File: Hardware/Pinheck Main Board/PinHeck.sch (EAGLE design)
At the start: 521 parts, among them IC2 PIC32MX795F512L-80I/PT, IC3 CD74HCT244E, IC4 CD74HCT244E, IC5 ULN2803A, J1 N/A, U1 P8X32A-Q44, U10 74HCT2G04GV,125, U11 74HC165D-Q100,118, U12 74HC165D-Q100,118, U13 CAT24M01LI-G, U14 MC74HC08ADR2G, U15 MC74HC08ADR2G, U16 MC74HC08ADR2G, U17 MC74HC08ADR2G, U18 MC74HC08ADR2G, U19 MC74HC08ADR2G, U2 DS1340Z-33+, U20 TIP107, U21 TIP107, U22 TIP107, U23 TIP107, U24 TIP107, U25 TIP107, U26 TIP107, U27 TIP107, U28 TIP102, U29 TIP102, U3 CD74HC595M96, U30 TIP102, U31 TIP102, U32 TIP102, U33 TIP102, U34 TIP102, U35 TIP102, U36 WS2801, U38 WS2801, U39 NCP1117DT33G, U4 CAT24M01LI-G, U5 CD74HC595M96, U52 CD74HC123M96, U6 TPS259251, U7 TPS259261, X1 FQ7050B-8.000, X2 9C-6.500MAAJ-T, X3 ABS25-32.768KHz-1-T

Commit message: Silkscreen done.
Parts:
- renumbered J1 to USB_PROG
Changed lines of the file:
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@@
 <grid distance="0.1" unitdist="inch" unit="inch" style="lines" multiple="1" display="no" altdistance="0.01" altunitdist="inch" altunit="inch"/>
 <layers>
-<layer number="1" name="Top" color="4" fill="1" visible="yes" active="no"/>
-<layer number="2" name="Route2" color="1" fill="3" visible="yes" active="no"/>
-<layer number="3" name="Route3" color="4" fill="3" visible="yes" active="no"/>
-<layer number="4" name="Route4" color="1" fill="4" visible="yes" active="no"/>
-<layer number="5" name="Route5" color="4" fill="4" visible="yes" active="no"/>
-<layer number="6" name="Route6" color="1" fill="8" visible="yes" active="no"/>
-<layer number="7" name="Route7" color="4" fill="8" visible="yes" active="no"/>
-<layer number="8" name="Route8" color="1" fill="2" visible="yes" active="no"/>
-<layer number="9" name="Route9" color="4" fill="2" visible="yes" active="no"/>
-<layer number="10" name="Route10" color="1" fill="7" visible="yes" active="no"/>
-<layer number="11" name="Route11" color="4" fill="7" visible="yes" active="no"/>
-<layer number="12" name="Route12" color="1" fill="5" visible="yes" active="no"/>
-<layer number="13" name="Route13" color="4" fill="5" visible="yes" active="no"/>
-<layer number="14" name="Route14" color="13" fill="6" visible="yes" active="no"/>
-<layer number="15" name="Route15" color="4" fill="6" visible="yes" active="no"/>
-<layer number="16" name="Bottom" color="1" fill="1" visible="yes" active="no"/>
-<layer number="17" name="Pads" color="2" fill="1" visible="yes" active="no"/>
-<layer number="18" name="Vias" color="2" fill="1" visible="yes" active="no"/>
-<layer number="19" name="Unrouted" color="6" fill="1" visible="yes" active="no"/>
-<layer number="20" name="Dimension" color="15" fill="1" visible="yes" active="no"/>
-<layer number="21" name="tPlace" color="7" fill="1" visible="yes" active="no"/>
-<layer number="22" name="bPlace" color="7" fill="1" visible="yes" active="no"/>
-<layer number="23" name="tOrigins" color="15" fill="1" visible="yes" active="no"/>
-<layer number="24" name="bOrigins" color="15" fill="1" visible="yes" active="no"/>
-<layer number="25" name="tNames" color="7" fill="1" visible="yes" active="no"/>
-<layer number="26" name="bNames" color="7" fill="1" visible="yes" active="no"/>
-<layer number="27" name="tValues" color="7" fill="1" visible="yes" active="no"/>
-<layer number="28" name="bValues" color="7" fill="1" visible="yes" active="no"/>
+<layer number="1" name="Top" color="4" fill="1" visible="no" active="no"/>
+<layer number="2" name="Route2" color="1" fill="3" visible="no" active="no"/>
+<layer number="3" name="Route3" color="4" fill="3" visible="no" active="no"/>
+<layer number="4" name="Route4" color="1" fill="4" visible="no" active="no"/>
+<layer number="5" name="Route5" color="4" fill="4" visible="no" active="no"/>
+<layer number="6" name="Route6" color="1" fill="8" visible="no" active="no"/>
+<layer number="7" name="Route7" color="4" fill="8" visible="no" active="no"/>
+<layer number="8" name="Route8" color="1" fill="2" visible="no" active="no"/>
+<layer number="9" name="Route9" color="4" fill="2" visible="no" active="no"/>
+<layer number="10" name="Route10" color="1" fill="7" visible="no" active="no"/>
+<layer number="11" name="Route11" color="4" fill="7" visible="no" active="no"/>
+<layer number="12" name="Route12" color="1" fill="5" visible="no" active="no"/>
+<layer number="13" name="Route13" color="4" fill="5" visible="no" active="no"/>
+<layer number="14" name="Route14" color="13" fill="6" visible="no" active="no"/>
+<layer number="15" name="Route15" color="4" fill="6" visible="no" active="no"/>
+<layer number="16" name="Bottom" color="1" fill="1" visible="no" active="no"/>
+<layer number="17" name="Pads" color="2" fill="1" visible="no" active="no"/>
+<layer number="18" name="Vias" color="2" fill="1" visible="no" active="no"/>
+<layer number="19" name="Unrouted" color="6" fill="1" visible="no" active="no"/>
+<layer number="20" name="Dimension" color="15" fill="1" visible="no" active="no"/>
+<layer number="21" name="tPlace" color="7" fill="1" visible="no" active="no"/>
+<layer number="22" name="bPlace" color="7" fill="1" visible="no" active="no"/>
+<layer number="23" name="tOrigins" color="15" fill="1" visible="no" active="no"/>
+<layer number="24" name="bOrigins" color="15" fill="1" visible="no" active="no"/>
+<layer number="25" name="tNames" color="7" fill="1" visible="no" active="no"/>
+<layer number="26" name="bNames" color="7" fill="1" visible="no" active="no"/>
+<layer number="27" name="tValues" color="7" fill="1" visible="no" active="no"/>
+<layer number="28" name="bValues" color="7" fill="1" visible="no" active="no"/>
 <layer number="29" name="tStop" color="7" fill="3" visible="no" active="no"/>
 <layer number="30" name="bStop" color="7" fill="6" visible="no" active="no"/>
@@
 <layer number="35" name="tGlue" color="7" fill="4" visible="no" active="no"/>
 <layer number="36" name="bGlue" color="7" fill="5" visible="no" active="no"/>
-<layer number="37" name="tTest" color="7" fill="1" visible="yes" active="no"/>
-<layer number="38" name="bTest" color="7" fill="1" visible="yes" active="no"/>
+<layer number="37" name="tTest" color="7" fill="1" visible="no" active="no"/>
+<layer number="38" name="bTest" color="7" fill="1" visible="no" active="no"/>
 <layer number="39" name="tKeepout" color="4" fill="11" visible="no" active="no"/>
 <layer number="40" name="bKeepout" color="1" fill="11" visible="no" active="no"/>
@@
 <layer number="44" name="Drills" color="7" fill="1" visible="no" active="no"/>
 <layer number="45" name="Holes" color="7" fill="1" visible="no" active="no"/>
-<layer number="46" name="Milling" color="3" fill="1" visible="yes" active="no"/>
-<layer number="47" name="Measures" color="7" fill="1" visible="yes" active="no"/>
-<layer number="48" name="Document" color="7" fill="1" visible="yes" active="no"/>
-<layer number="49" name="Reference" color="7" fill="1" visible="yes" active="no"/>
-<layer number="50" name="dxf" color="7" fill="1" visible="yes" active="no"/>
-<layer number="51" name="tDocu" color="7" fill="1" visible="yes" active="no"/>
-<layer number="52" name="bDocu" color="7" fill="1" visible="yes" active="no"/>
-<layer number="53" name="tGND_GNDA" color="7" fill="9" visible="yes" active="no"/>
-<layer number="54" name="bGND_GNDA" color="1" fill="9" visible="yes" active="no"/>
-<layer number="56" name="wert" color="7" fill="1" visible="yes" active="no"/>
+<layer number="46" name="Milling" color="3" fill="1" visible="no" active="no"/>
+<layer number="47" name="Measures" color="7" fill="1" visible="no" active="no"/>
+<layer number="48" name="Document" color="7" fill="1" visible="no" active="no"/>
+<layer number="49" name="Reference" color="7" fill="1" visible="no" active="no"/>
+<layer number="50" name="dxf" color="7" fill="1" visible="no" active="no"/>
+<layer number="51" name="tDocu" color="7" fill="1" visible="no" active="no"/>
+<layer number="52" name="bDocu" color="7" fill="1" visible="no" active="no"/>
+<layer number="53" name="tGND_GNDA" color="7" fill="9" visible="no" active="no"/>
+<layer number="54" name="bGND_GNDA" color="1" fill="9" visible="no" active="no"/>
+<layer number="56" name="wert" color="7" fill="1" visible="no" active="no"/>
 <layer number="91" name="Nets" color="2" fill="1" visible="yes" active="yes"/>
 <layer number="92" name="Busses" color="1" fill="1" visible="yes" active="yes"/>
@@
 <part name="C61" library="PP_Passives" deviceset="CAPACITOR_NON_POLAR" device="_0805" value="5.6nF"/>
 <part name="R157" library="PP_Passives" deviceset="RESISTOR" device="_0805" value="110K"/>
-<part name="J1" library="PP_Connectors" deviceset="CON_01X04" device="_2.54MM_PIN_HEADER" value="N/A">
+<part name="USB_PROG" library="PP_Connectors" deviceset="CON_01X04" device="_2.54MM_PIN_HEADER" value="N/A">
 <attribute name="LABEL01" value="VUSB"/>
 <attribute name="LABEL02" value="USB D-"/>
@@
 <instance part="C61" gate="G$1" x="746.76" y="210.82" rot="R270"/>
 <instance part="R157" gate="G$1" x="779.78" y="210.82"/>
-<instance part="J1" gate="G$1" x="370.84" y="129.54"/>
+<instance part="USB_PROG" gate="G$1" x="370.84" y="129.54"/>
 <instance part="D3" gate="G$1" x="731.52" y="238.76" rot="R90"/>
 <instance part="D4" gate="G$1" x="731.52" y="208.28" rot="R90"/>
@@
 </segment>
 <segment>
-<pinref part="J1" gate="G$1" pin="4"/>
+<pinref part="USB_PROG" gate="G$1" pin="4"/>
 <wire x1="368.3" y1="121.92" x2="358.14" y2="121.92" width="0.1524" layer="91"/>
 <label x="360.68" y="121.92" size="0.8128" layer="95" font="vector"/>
@@
 </segment>
 <segment>
-<pinref part="J1" gate="G$1" pin="3"/>
+<pinref part="USB_PROG" gate="G$1" pin="3"/>
 <wire x1="358.14" y1="124.46" x2="368.3" y2="124.46" width="0.1524" layer="91"/>
 <label x="360.68" y="124.46" size="0.8128" layer="95" font="vector"/>
@@
 </segment>
 <segment>
-<pinref part="J1" gate="G$1" pin="2"/>
+<pinref part="USB_PROG" gate="G$1" pin="2"/>
 <wire x1="368.3" y1="127" x2="358.14" y2="127" width="0.1524" layer="91"/>
 <label x="360.68" y="127" size="0.8128" layer="95" font="vector"/>
@@
 </segment>
 <segment>
-<pinref part="J1" gate="G$1" pin="1"/>
+<pinref part="USB_PROG" gate="G$1" pin="1"/>
 <wire x1="368.3" y1="129.54" x2="358.14" y2="129.54" width="0.1524" layer="91"/>
 <label x="360.68" y="129.54" size="0.8128" layer="95" font="vector"/>

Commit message: REV 7 preliminary done.
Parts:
- added 3.3V: (no value), PP_Connectors:TEST_POINT_SINGLE_ROUND_100MIL
- added FID1, FID2, FID3: FIDUCIAL_100MIL, MF_Aesthetics:FIDUCIAL_100MIL
- added FID4, FID5: FIDUCIAL_0.5MM, MF_Aesthetics:FIDUCIAL_0.5MM
- renumbered BOARD_POWER to BOARD_POWER_IN, CABINET to CABINET_I/O, PIC_RST to PIC_RESET, PROP_RST to PROP_RESET, SOL_PWR to SOLENOID_POWER_IN
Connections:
- net 3.3V: now also 3.3V.P$1

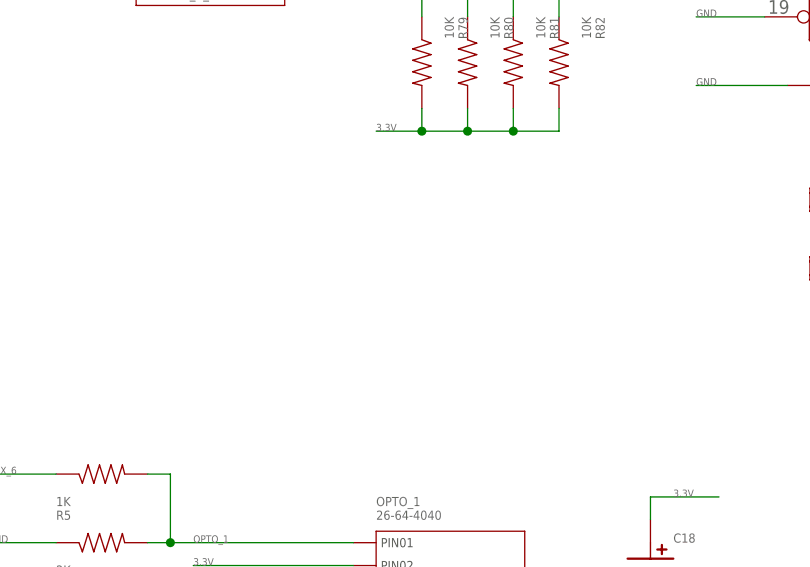
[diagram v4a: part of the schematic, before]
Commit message: Added AUX power Connector
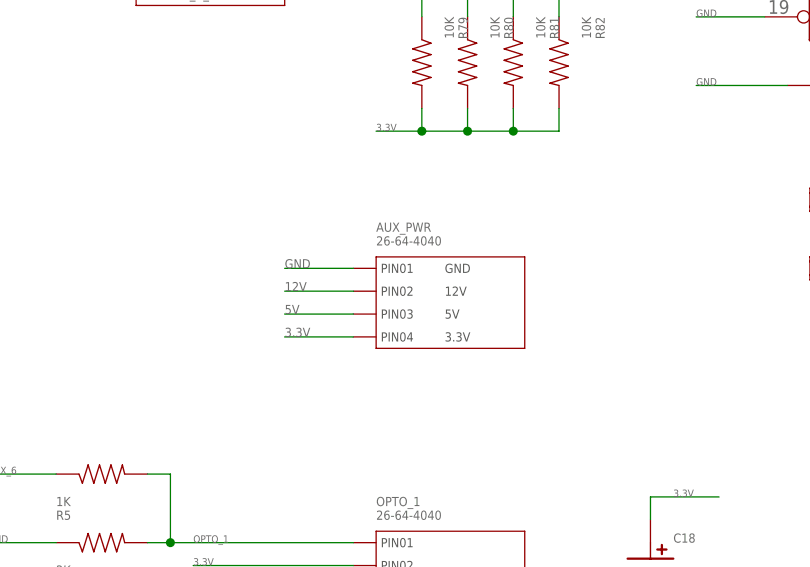
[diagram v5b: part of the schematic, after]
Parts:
- added AUX_PWR: 26-64-4040, PP_Connectors:CON_01X04_26-64-4040
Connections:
- net 12V: now also AUX_PWR.2
- net 3.3V: now also AUX_PWR.4
- net 5V: now also AUX_PWR.3
- net GND: now also AUX_PWR.1
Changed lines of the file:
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@@
 <part name="FID5" library="MF_Aesthetics" deviceset="FIDUCIAL" device="_0.5MM"/>
 <part name="3.3V" library="PP_Connectors" deviceset="TEST_POINT_SINGLE" device="_ROUND_100MIL"/>
+<part name="AUX_PWR" library="PP_Connectors" deviceset="CON_01X04" device="_26-64-4040" value="26-64-4040">
+<attribute name="LABEL01" value="GND"/>
+<attribute name="LABEL02" value="12V"/>
+<attribute name="LABEL03" value="5V"/>
+<attribute name="LABEL04" value="3.3V"/>
+</part>
 </parts>
 <sheets>
@@
 <instance part="FID5" gate="G$1" x="845.82" y="-58.42"/>
 <instance part="3.3V" gate="G$1" x="-43.18" y="-101.6" rot="R180"/>
+<instance part="AUX_PWR" gate="G$1" x="637.54" y="-33.02"/>
 </instances>
 <busses>
@@
 <label x="-93.98" y="30.48" size="1.016" layer="95" font="vector"/>
 </segment>
+<segment>
+<pinref part="AUX_PWR" gate="G$1" pin="1"/>
+<wire x1="635" y1="-33.02" x2="627.38" y2="-33.02" width="0.1524" layer="91"/>
+<label x="627.38" y="-33.02" size="1.016" layer="95" font="vector"/>
+</segment>
 </net>
 <net name="RX_PIC32" class="0">
@@
 <label x="-38.1" y="-101.6" size="1.016" layer="95" font="vector"/>
 </segment>
+<segment>
+<pinref part="AUX_PWR" gate="G$1" pin="4"/>
+<wire x1="627.38" y1="-40.64" x2="635" y2="-40.64" width="0.1524" layer="91"/>
+<label x="627.38" y="-40.64" size="1.016" layer="95" font="vector"/>
+</segment>
 </net>
 <net name="RES" class="0">
@@
 <label x="787.4" y="251.46" size="0.8128" layer="95" font="vector"/>
 </segment>
+<segment>
+<pinref part="AUX_PWR" gate="G$1" pin="3"/>
+<wire x1="635" y1="-38.1" x2="627.38" y2="-38.1" width="0.1524" layer="91"/>
+<label x="627.38" y="-38.1" size="1.016" layer="95" font="vector"/>
+</segment>
 </net>
 <net name="CAB_LAT" class="0">
@@
 <label x="787.4" y="220.98" size="0.8128" layer="95" font="vector"/>
 </segment>
+<segment>
+<pinref part="AUX_PWR" gate="G$1" pin="2"/>
+<wire x1="627.38" y1="-35.56" x2="635" y2="-35.56" width="0.1524" layer="91"/>
+<label x="627.38" y="-35.56" size="1.016" layer="95" font="vector"/>
+</segment>
 </net>
